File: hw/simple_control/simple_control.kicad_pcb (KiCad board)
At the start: 4 copper layers, 99.1 x 99.1 mm, 87 parts, among them J101 Screw_Terminal_01x02, J102 Jack-DC, J103 Screw_Terminal_01x03, J104 Screw_Terminal_01x03, J1301 Micro_SD_Card, J1401 Conn_02x05_Odd_Even, J601 Conn_01x04, J602 Raspberry_Pi_0_2_3, J603 Conn_01x03, Q1001 BC817, Q201 AOSP21357, Q701 BC817, Q801 BC817, Q901 BC817, SW1201 SW_Push, SW601 SW_Push, U1101 CAT24C256, U301 SN74AHCT125D, U601 PicoW

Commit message: chore(hw): fix footprints
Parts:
- C201: footprint Jumper:SolderJumper-2_P1.3mm_Open_RoundedPad1.0x1.5mm -> Capacitor_SMD:C_0805_2012Metric_Pad1.18x1.45mm_HandSolder
- moved R1002 146.2 mm to (28.4, 111.3)
- moved R701 146.2 mm to (28.4, 120.8)
- moved R702 146.2 mm to (28.4, 123.7)
- moved R901 146.2 mm to (28.4, 133.2)
- moved R902 146.2 mm to (28.4, 136.2)
- moved C1101 146.2 mm to (48.3, 116.7)
- moved C1201 146.2 mm to (81.3, 128.4)
- moved C1301 146.2 mm to (43.6, 98.0)
- moved C1401 146.2 mm to (50.8, 121.7)
- moved C1402 146.2 mm to (50.8, 124.7)
- moved C601 146.2 mm to (80.7, 86.7)
- moved C602 146.2 mm to (80.7, 89.7)
- moved C603 146.2 mm to (80.7, 92.8)
- moved D1001 146.2 mm to (33.2, 108.4)
- moved D701 146.2 mm to (33.2, 120.8)
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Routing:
- net Net-(U301-3~{OE}): track 6.83 -> 6.06 mm

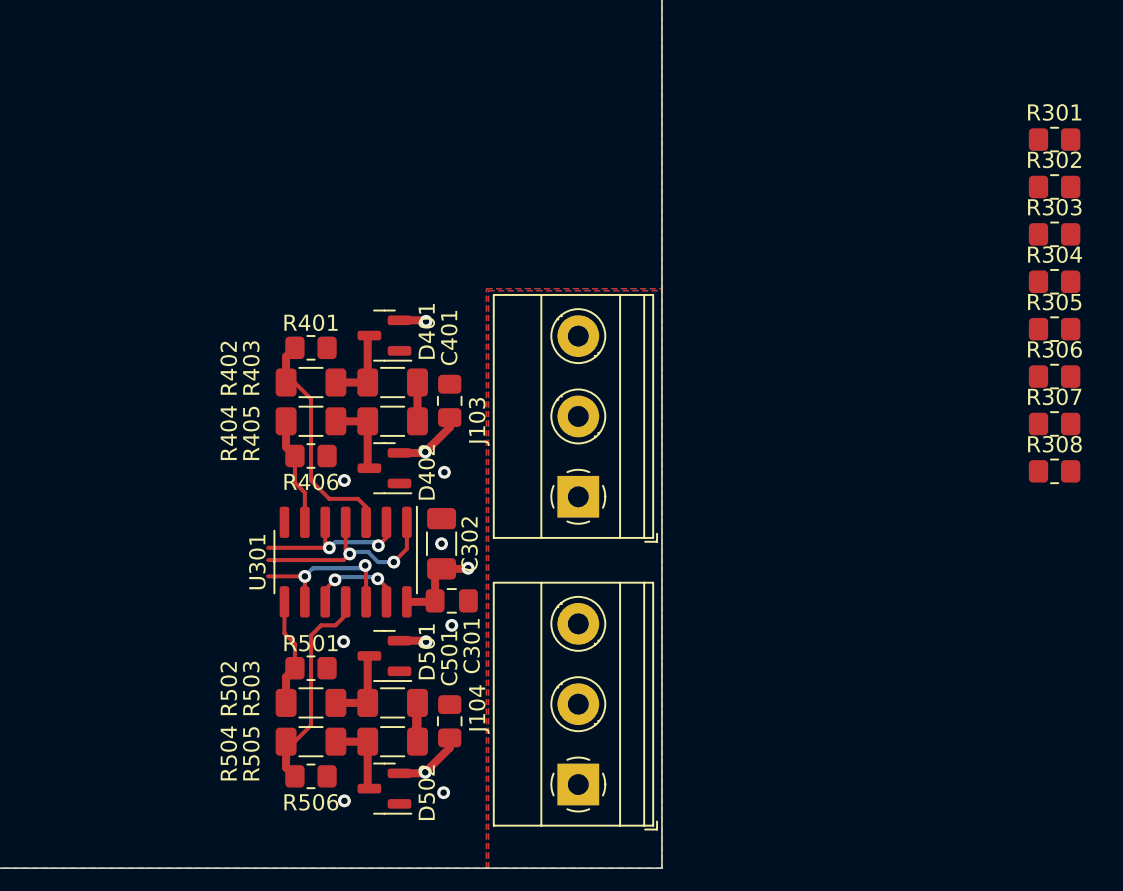
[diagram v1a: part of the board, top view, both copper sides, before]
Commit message: chore(hw): add LED driver stage layout
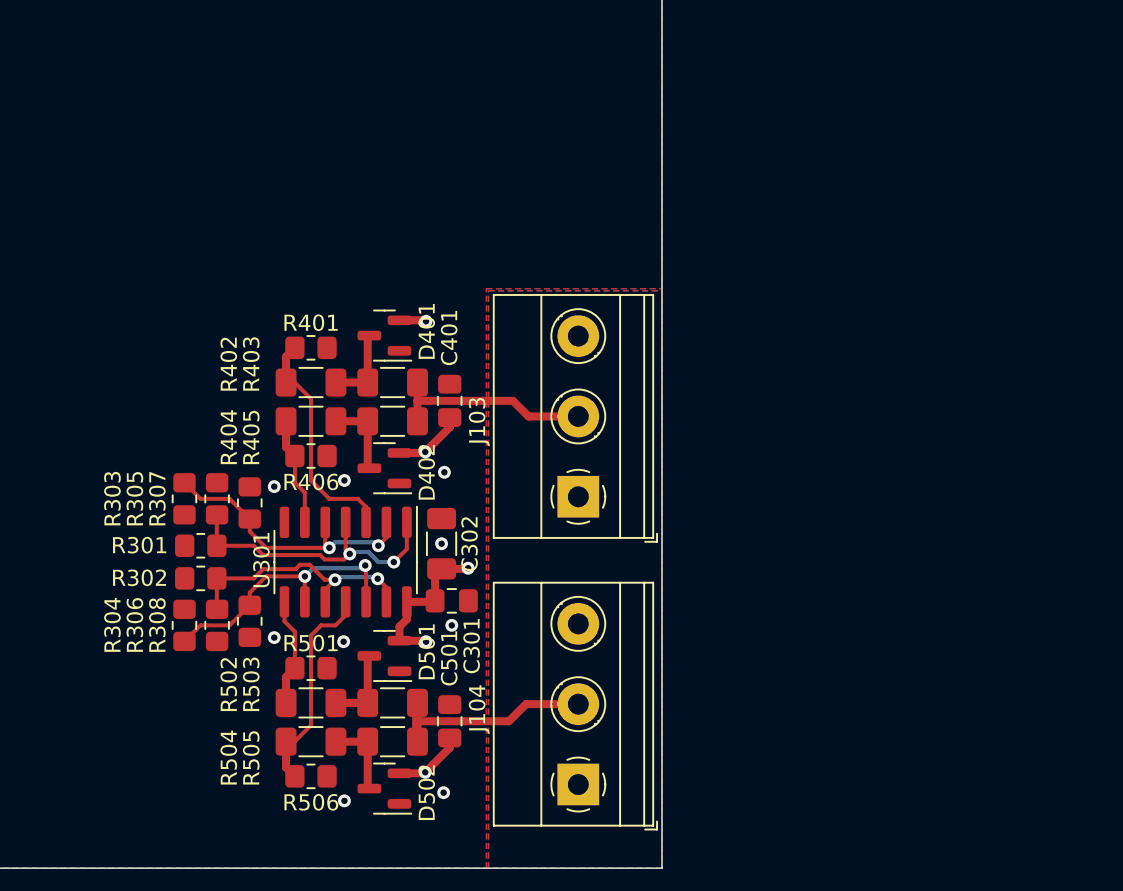
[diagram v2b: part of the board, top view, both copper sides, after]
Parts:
- moved R301 58.8 mm to (172.0, 119.6)
- moved R302 58.5 mm to (172.0, 121.7)
- moved R304 58.2 mm to (170.9, 124.6), turned to -90 degrees
- moved R303 56.6 mm to (170.9, 116.7), turned to 90 degrees
- moved R306 54.4 mm to (173.0, 124.6), turned to -90 degrees
- moved R305 53.2 mm to (173.0, 116.7), turned to 90 degrees
- moved R308 51.0 mm to (175.0, 124.3), turned to -90 degrees
- moved R307 50.3 mm to (175.0, 117.0), turned to 90 degrees
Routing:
- net /LED Driver/DATA_OUT1: track 9.65 -> 20.2 mm
- net /LED Driver/DATA_OUT0: track 2.41 -> 12.8 mm
- net Net-(U301-3~{OE}): track 6.06 -> 16.1 mm
- net Net-(U301-1A): track 10.4 -> 17.8 mm
- net Net-(U301-3A): track 10.2 -> 17.5 mm
- net Net-(U301-1~{OE}): track 13.2 -> 18.6 mm
- net +5V: track 29.1 -> 31.7 mm
- net GND: vias 8 -> 10

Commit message: chore(hw): add led driver layout
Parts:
- moved R303 3.45 mm to (174.2, 117.7), turned to 0 degrees
- moved R304 3.45 mm to (174.2, 123.6), turned to 0 degrees
- moved R301 2.29 mm to (174.2, 119.6)
- moved R302 2.29 mm to (174.2, 121.7)
- moved R308 2.16 mm to (174.9, 126.5)
- moved R307 2.16 mm to (174.9, 114.8)
- moved R306 1.91 mm to (172.8, 126.5)
- moved R305 1.91 mm to (172.8, 114.8)
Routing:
- net +5V: track 31.7 -> 50.2 mm
- net Net-(U301-1A): track 17.8 -> 14.7 mm
- net Net-(U301-3A): track 17.5 -> 14.5 mm
- net Net-(U301-3~{OE}): track 16.1 -> 16.7 mm
- net Net-(U301-1~{OE}): track 18.6 -> 19.3 mm

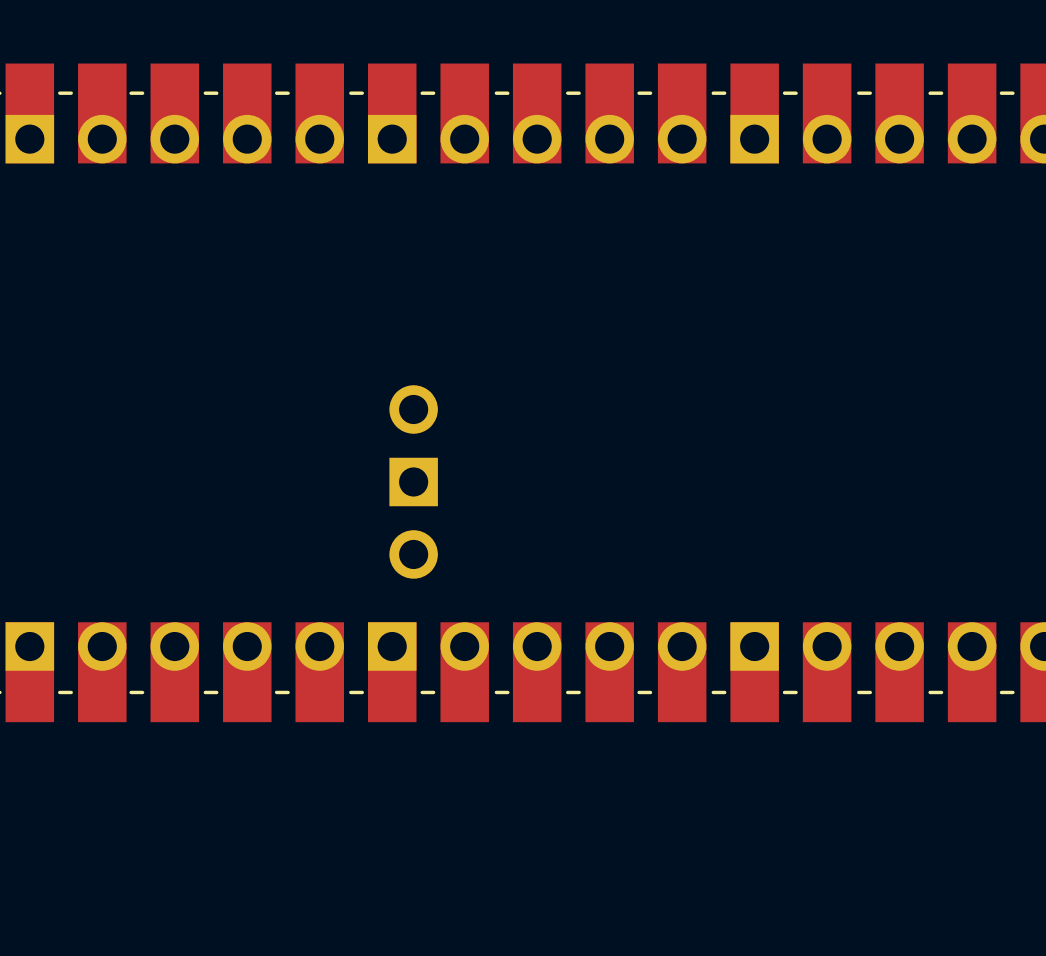
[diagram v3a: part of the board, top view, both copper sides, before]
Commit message: chore(hw): layout module interconnects
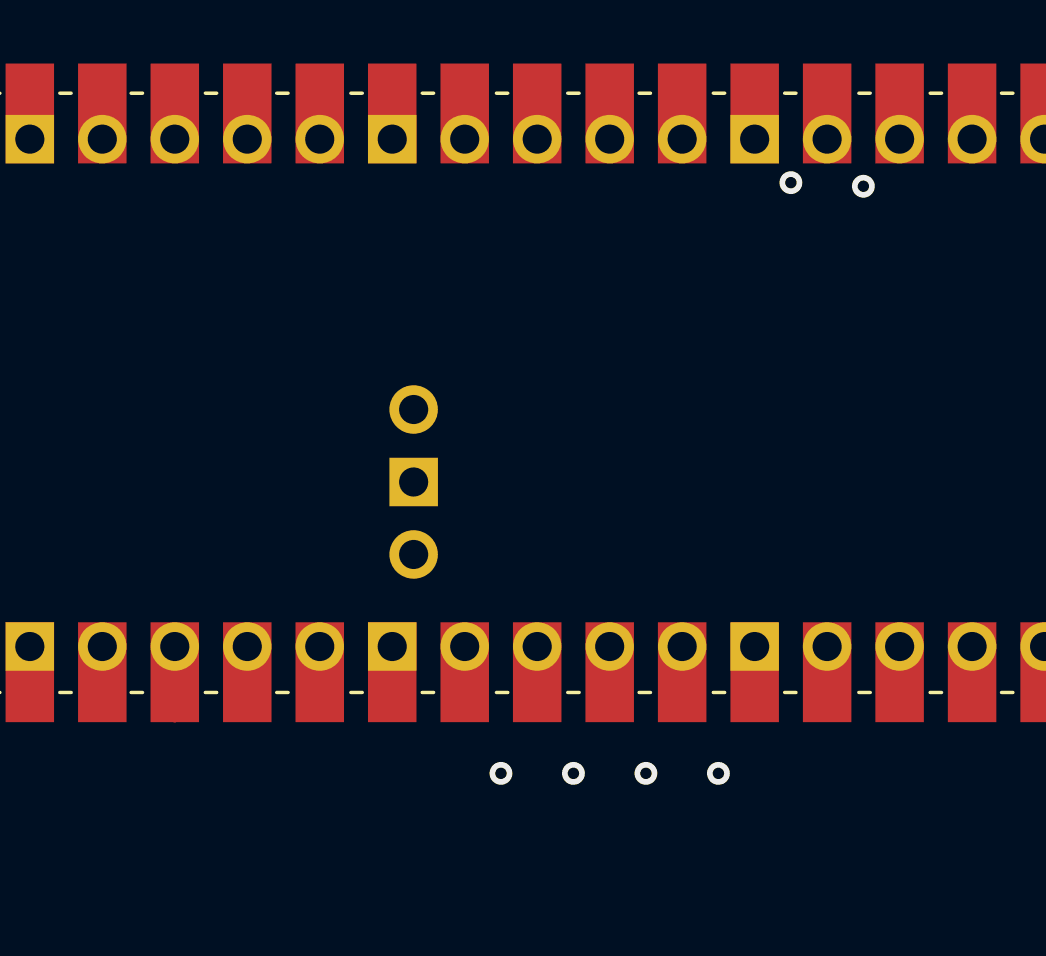
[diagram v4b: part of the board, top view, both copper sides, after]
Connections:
- U601 pad 10: /LED_DATA_~{EN}0 -> /CPU/STAT_LED1
- U601 pad 11: /CPU/PRIM_LED_DATA1 -> /CPU/STAT_LED2
- U601 pad 12: /LED_DATA_~{EN}1 -> /CPU/STAT_LED3
- U601 pad 14: /CPU/STAT_LED0 -> /CPU/PRIM_LED_DATA0
- U601 pad 15: /CPU/STAT_LED1 -> /LED_DATA_~{EN}0
- U601 pad 16: /CPU/STAT_LED2 -> /CPU/PRIM_LED_DATA1
- U601 pad 17: /CPU/STAT_LED3 -> /LED_DATA_~{EN}1
- U601 pad 9: /CPU/PRIM_LED_DATA0 -> /CPU/STAT_LED0
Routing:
- net /CPU/SPI_FLASH_MISO: track 0.00 -> 63.2 mm, vias 0 -> 1
- net /CPU/SPI_FLASH_~{CS}: track 0.00 -> 59.5 mm, vias 0 -> 1
- net /CPU/SPI_FLASH_MOSI: track 0.00 -> 58.9 mm, vias 0 -> 1
- net /CPU/SPI_FLASH_CLK: track 0.00 -> 49.3 mm, vias 0 -> 1
- net /LED_DATA_~{EN}0: track 0.00 -> 33.9 mm, vias 0 -> 1
- net /CPU/RTC_GPIO: track 0.00 -> 28.6 mm
- net /CPU/ID_SCL: track 0.00 -> 26.2 mm
- net /CPU/ID_SDA: track 0.00 -> 24.8 mm
- net +3.3V: track 0.00 -> 24.4 mm
- net /CPU/STAT_LED2: track 0.00 -> 24.1 mm
- net /CPU/STAT_LED3: track 0.00 -> 23.3 mm, vias 0 -> 1
- net /CPU/TERM_TXD: track 0.00 -> 21.2 mm
- net /CPU/CPU_BUTTON: track 0.00 -> 20.2 mm
- net /CPU/TERM_RXD: track 0.00 -> 18.5 mm
- net /CPU/PRIM_LED_DATA0: track 0.00 -> 12.3 mm
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- added copper zone on In2.Cu, net +3.3V

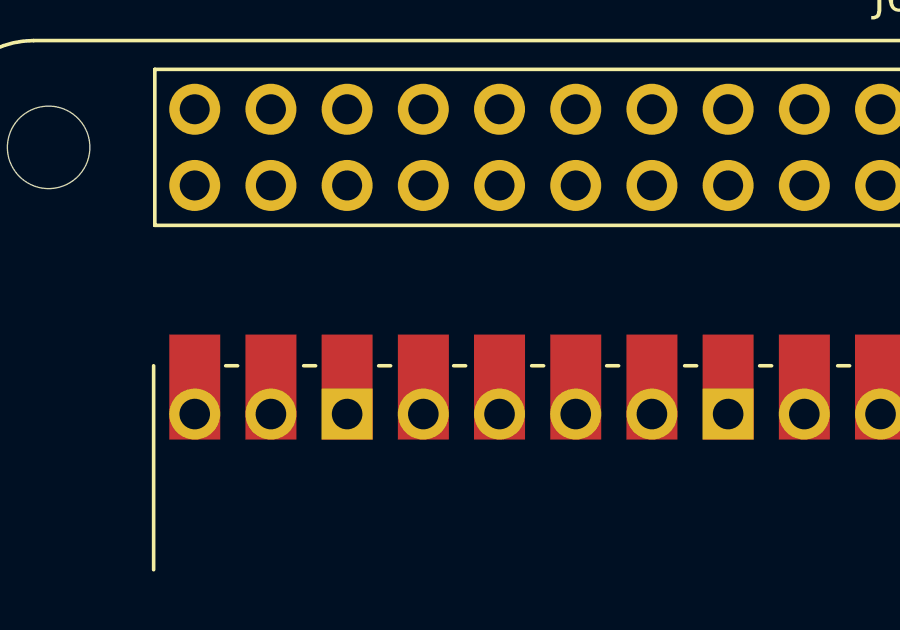
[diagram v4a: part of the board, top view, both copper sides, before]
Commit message: chore(hw): add more button connections with interconnections layout
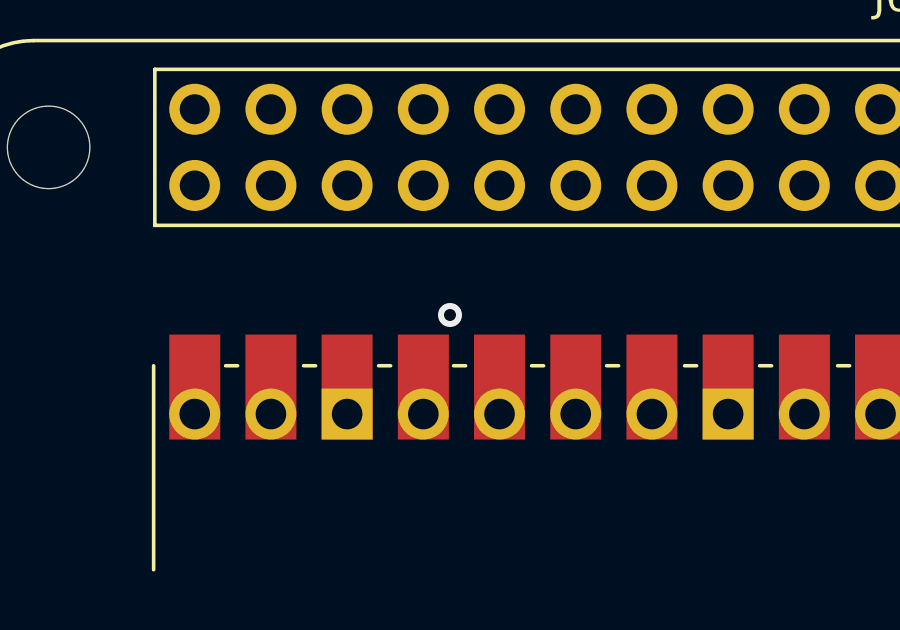
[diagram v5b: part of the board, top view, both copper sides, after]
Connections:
- C1201 pad 1: /CPU/CPU_BUTTON -> /CPU/Filtered Button/SW
- J602 pad 29: unconnected-(J602-GCLK1/GPIO5-Pad29) -> /CPU/BUTTON0
- J602 pad 31: /CPU/CPU_BUTTON -> /CPU/BUTTON1
- J602 pad 35: unconnected-(J602-GPIO19/MISO1-Pad35) -> /CPU/BUTTON3
- J602 pad 40: unconnected-(J602-GPIO21/SCLK1-Pad40) -> /CPU/BUTTON2
- R1202 pad 2: /CPU/CPU_BUTTON -> /CPU/Filtered Button/SW
- U601 pad 19: /CPU/CPU_BUTTON -> /CPU/BUTTON3
- U601 pad 26: unconnected-(U601-GPIO20-Pad26) -> /CPU/BUTTON2
- U601 pad 27: unconnected-(U601-GPIO21-Pad27) -> /CPU/BUTTON1
- U601 pad 29: unconnected-(U601-GPIO22-Pad29) -> /CPU/BUTTON0
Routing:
- net /CPU/BUTTON2: track 0.00 -> 35.6 mm, vias 0 -> 1
- net /CPU/BUTTON0: track 0.00 -> 28.6 mm
- net /CPU/BUTTON1: track 0.00 -> 27.5 mm
- net /CPU/CPU_BUTTON: track 20.2 -> 0.00 mm
- net /CPU/BUTTON3: track 0.00 -> 8.67 mm
- net +5V: track 50.2 -> 58.2 mm
- net /CPU/SPI_FLASH_MOSI: track 58.9 -> 56.3 mm
- net /CPU/SPI_FLASH_MISO: track 63.2 -> 62.4 mm
- net /CPU/SPI_FLASH_CLK: track 49.3 -> 48.7 mm

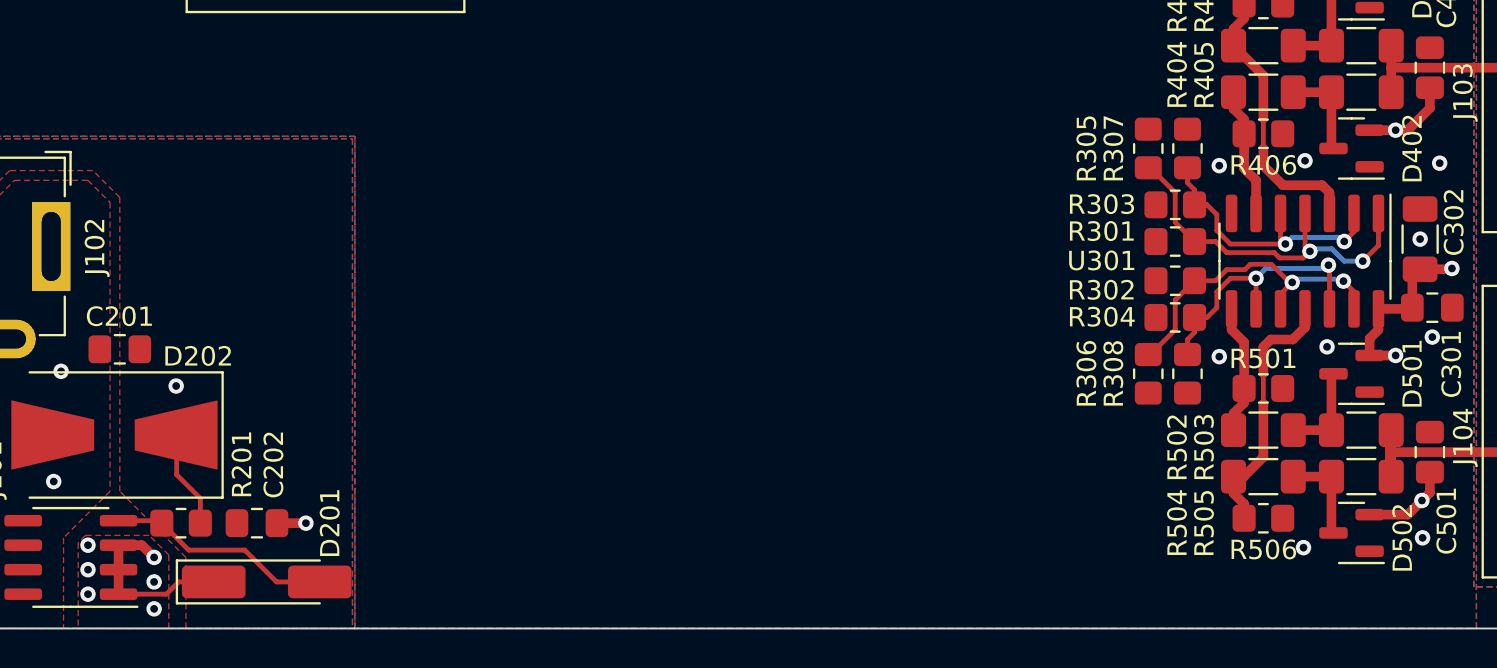
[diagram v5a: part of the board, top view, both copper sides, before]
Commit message: chore(hw): switch to 0.3 mm traces by default
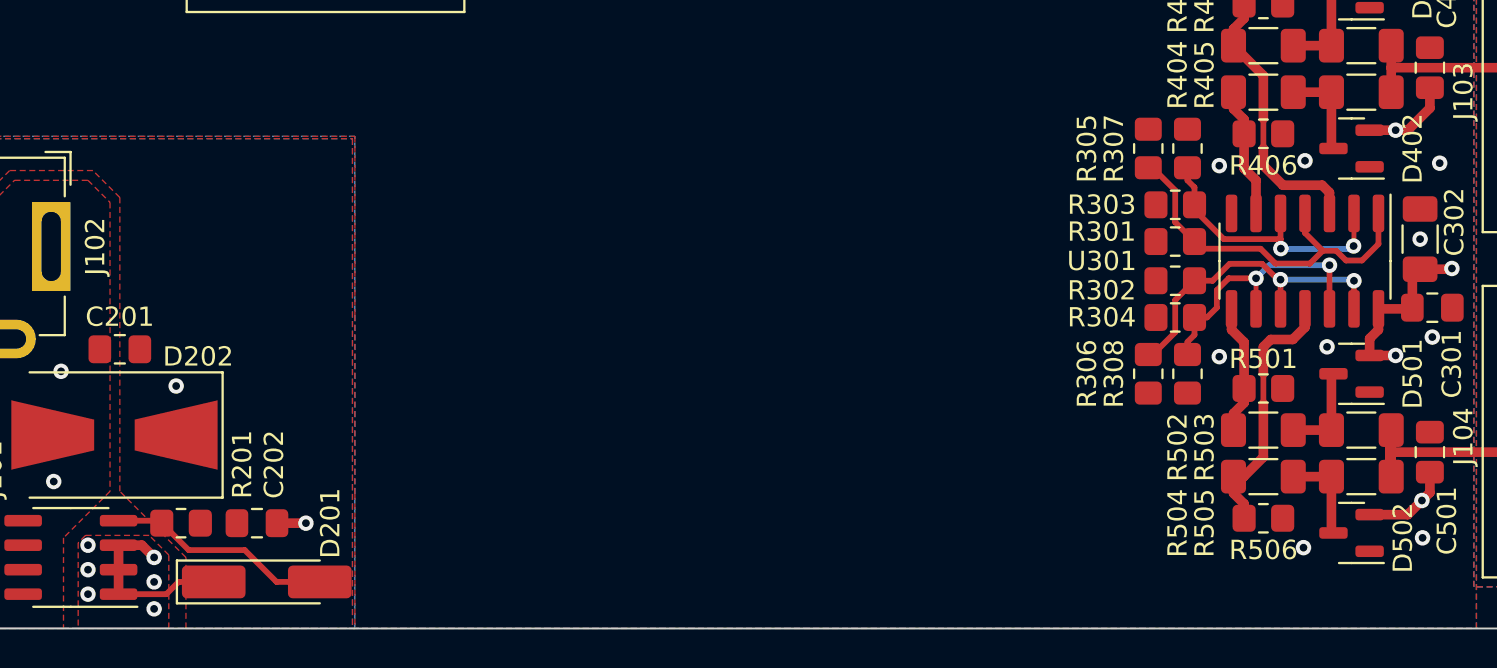
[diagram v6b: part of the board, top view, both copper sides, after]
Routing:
- net GND: track 5.08 -> 0.00 mm
- net /CPU/SPI_FLASH_~{CS}: track 59.5 -> 58.0 mm
- net /CPU/SPI_FLASH_MISO: track 62.4 -> 61.0 mm
- net Net-(U301-1~{OE}): track 19.3 -> 19.7 mm, vias 2 -> 0
